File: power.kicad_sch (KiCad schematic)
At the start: 21 parts, among them U10 RT9080-33GJ5, U11 AP22804AW5, U8 TPS2120YFPR, U9 RT9080-33GJ5

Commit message: Membuat library dan memperbaiki footprint pada schematic
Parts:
- U8: footprint Package_BGA:Texas_YFP0020_DSBGA-20_1.56x1.96mm_Layout4x5_P0.4mm -> Package_BGA:Texas_YFP0020_DSBGA-20_1.588x1.988mm_Layout4x5_P0.4mm
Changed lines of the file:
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@@
 			)
 		)
-		(property "Footprint" "Package_BGA:Texas_YFP0020_DSBGA-20_1.56x1.96mm_Layout4x5_P0.4mm"
+		(property "Footprint" "Package_BGA:Texas_YFP0020_DSBGA-20_1.588x1.988mm_Layout4x5_P0.4mm"
 			(at 68.58 83.82 0)
 			(hide yes)

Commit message: Mulai layout
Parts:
- added C46, C49, C50: 100n, Capacitor_SMD:C_0402_1005Metric, symbol Device:C
- added C47, C48: 4u7, Capacitor_SMD:C_0603_1608Metric, symbol Device:C
- added C51: 10u, Capacitor_SMD:C_0603_1608Metric, symbol Device:C
- added D6, D7: SMAJ6.0A, Diode_SMD:D_SMA, symbol Diode:SMAJ6.0A
- added R75, R76: 100k, Resistor_SMD:R_0402_1005Metric, symbol Device:R
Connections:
- net +5V_IN: now also C50.1, C51.1
- net +VBRICK1: now also C46.1, C47.1, D6.1 (A1)
- net +VBRICK2: now also C48.1, C49.1, D7.1 (A1)
- net GND: now also C46.2, C47.2, C48.2, C49.2, C50.2, C51.2, D6.2 (A2), D7.2 (A2), R75.2, R76.2
- net PERI_EN: now also R76.1
- net PWR_SEL: now also R75.1
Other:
- moved on the sheet: C34, C35, C36, C37, C38, C39, C40, C41, D4, R11, R12, R13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

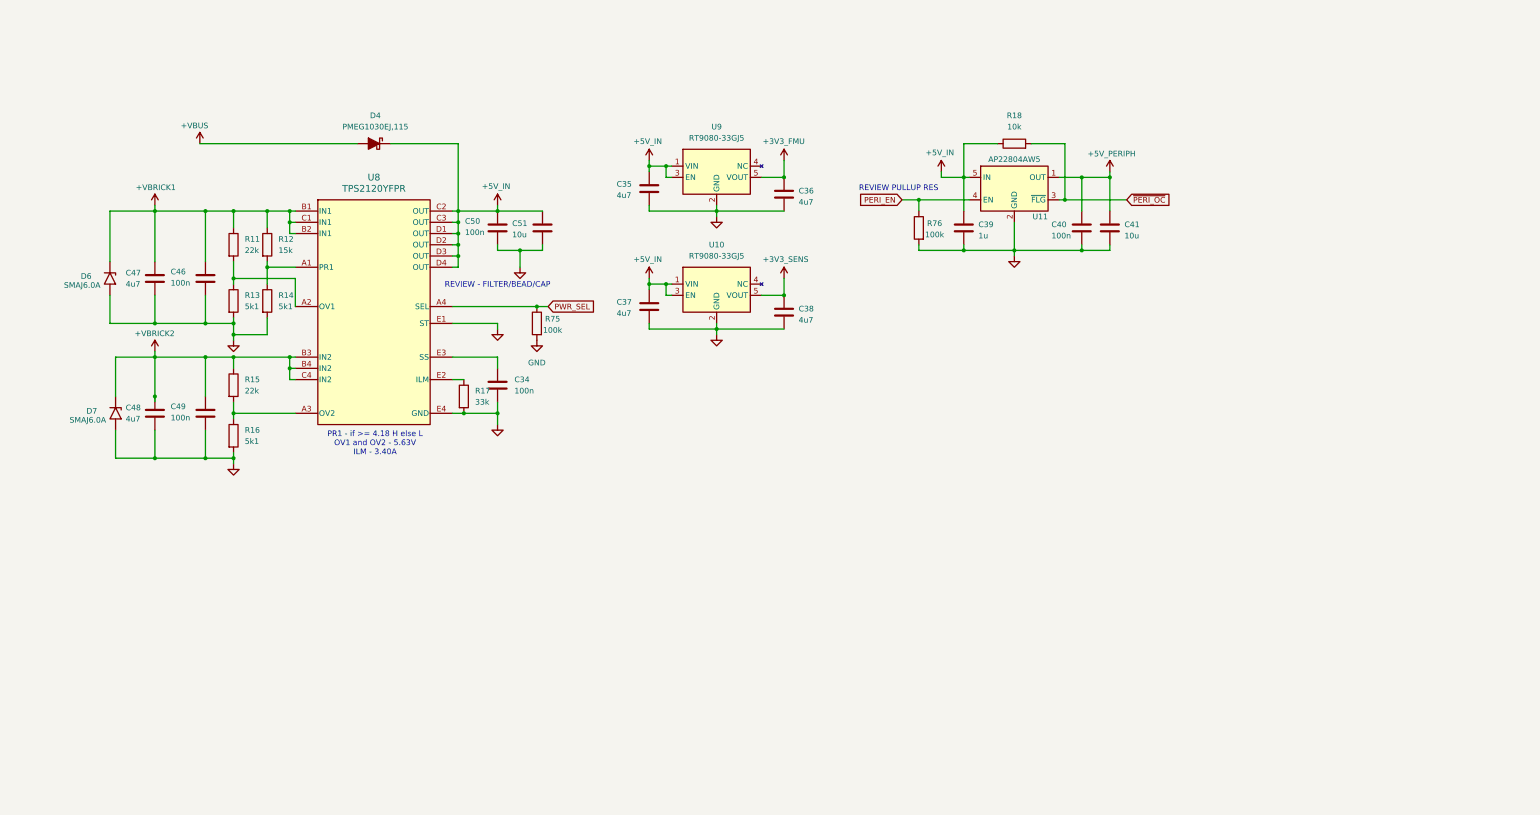
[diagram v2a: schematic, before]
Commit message: Schematic: sensor redundancy + blok current limiter GPS (terverifikasi)
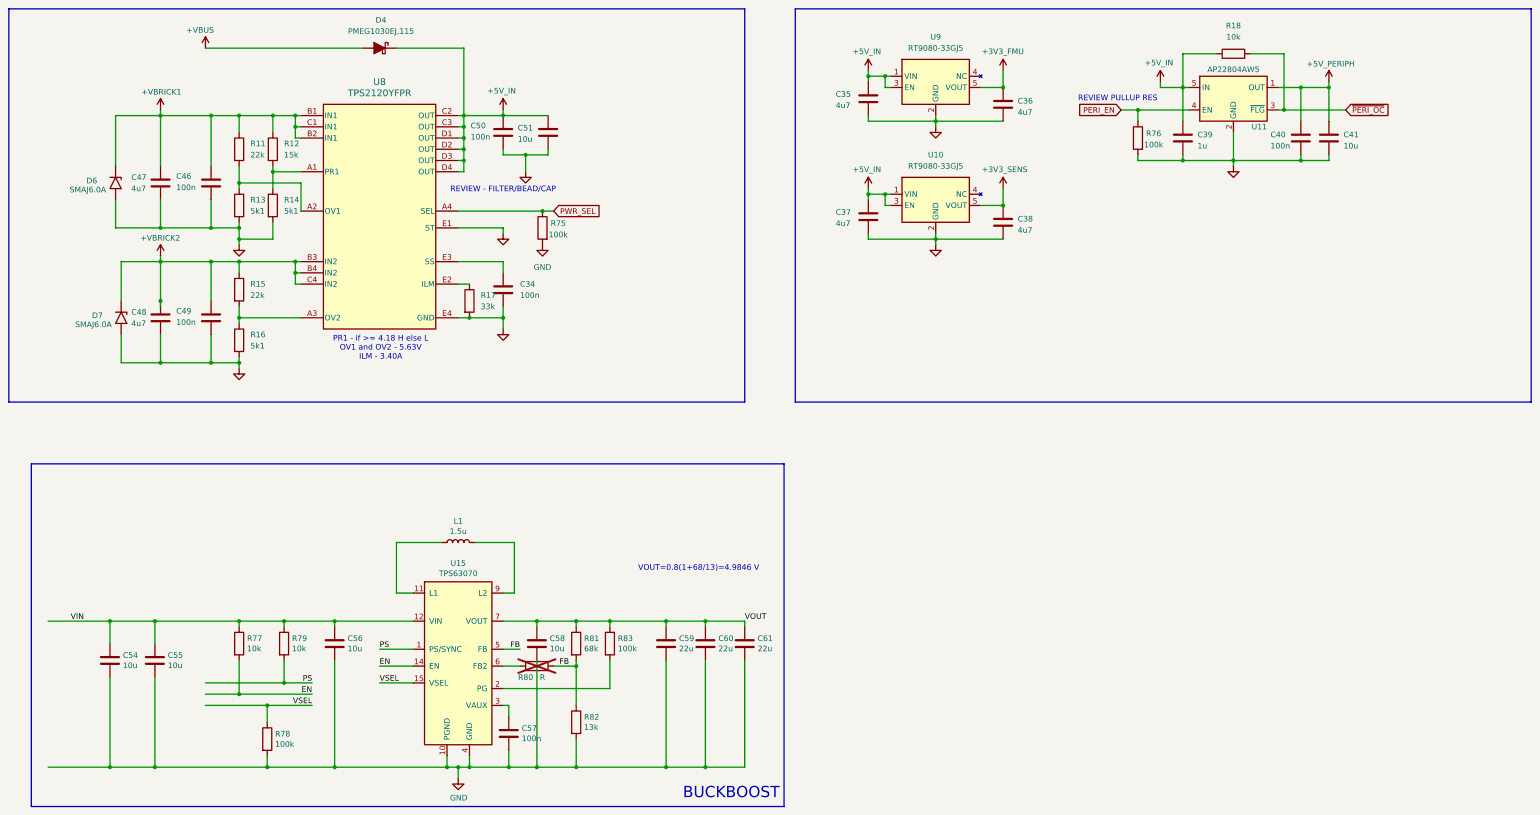
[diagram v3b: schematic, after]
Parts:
- added C54, C55: 10u, Capacitor_SMD:C_0805_2012Metric_Pad1.15x1.40mm_HandSolder, symbol Device:C
- added C56, C58: 10u, Capacitor_SMD:C_0603_1608Metric_Pad1.05x0.95mm_HandSolder, symbol Device:C
- added C57: 100n, Capacitor_SMD:C_0805_2012Metric_Pad1.15x1.40mm_HandSolder, symbol Device:C
- added C59, C60, C61: 22u, Capacitor_SMD:C_0805_2012Metric_Pad1.15x1.40mm_HandSolder, symbol Device:C
- added L1: 1.5u, tps63070:L_Coilcraft_XxL4020, symbol Device:L
- added R77, R79: 10k, Resistor_SMD:R_0805_2012Metric_Pad1.15x1.40mm_HandSolder, symbol Device:R
- added R78, R83: 100k, Resistor_SMD:R_0805_2012Metric_Pad1.15x1.40mm_HandSolder, symbol Device:R
- added R80: R, Resistor_SMD:R_0805_2012Metric_Pad1.15x1.40mm_HandSolder, symbol Device:R
- added R81: 68k, Resistor_SMD:R_0805_2012Metric_Pad1.15x1.40mm_HandSolder, symbol Device:R
- added R82: 13k, Resistor_SMD:R_0805_2012Metric_Pad1.15x1.40mm_HandSolder, symbol Device:R
- added U15: TPS63070, tps63070:VQFN-HR-15, symbol tps63070:tps63070
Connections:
- net GND: now also C54.2, C55.2, C56.2, C57.1, C58.2, C59.2, C60.2, C61.2, R78.2, R82.2, U15.10 (PGND), U15.4 (GND)
- new net: L1.1, U15.11 (L1)
- new net: R83.2, U15.2 (PG)
- new net: C57.2, U15.3 (VAUX)
- new net: R80.2, U15.6 (FB2)
- new net: L1.2, U15.9 (L2)
- new net EN: R77.2, U15.14 (EN)
- new net FB: R80.1, R81.2, R82.1, U15.5 (FB)
- new net PS: R79.2, U15.1 (PS/SYNC)
- new net VIN: C54.1, C55.1, C56.1, R77.1, R79.1, U15.12 (VIN)
- new net VOUT: C58.1, C59.1, C60.1, C61.1, R81.1, R83.1, U15.7 (VOUT)
- new net VSEL: R78.1, U15.15 (VSEL)
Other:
- note added: "BUCKBOOST"
- note added: "VOUT​=0.8(1+68/13)=4.9846 V​"
- moved on the sheet: C34, C35, C36, C37, C38, C39, C40, C41, C46, C47, C48, C49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

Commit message: Power: fix label VIN_BB/EN - U15.VIN kini driven; ERC 54
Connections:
- net VOUT is gone; now on net +5V_IN: C58.1, C59.1, C60.1, C61.1, R81.1, R83.1, U15.7 (VOUT)
- net +5V_IN: no longer C50.1, C51.1, D4.1 (K), U8.C2 (OUT), U8.C3 (OUT), U8.D1 (OUT), U8.D2 (OUT), U8.D3 (OUT), U8.D4 (OUT)
- net VIN renamed VIN_BB
- net VIN_BB: now also C50.1, C51.1, D4.1 (K), U8.C2 (OUT), U8.C3 (OUT), U8.D1 (OUT), U8.D2 (OUT), U8.D3 (OUT), U8.D4 (OUT)
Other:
- note added: "MAX IOUT = 2A"
- moved on the sheet: C54, C55, C56, C57, C58, C59, C60, C61, L1, R77, R78, R79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

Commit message: ERC: R80 DNP+100k+fp, Pin Conflicts Map lengkap; 0 errors / 17 lib-warnings (netlist diff 0, verified)
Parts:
- C54, C55, C57, C59, C60, C61: footprint Capacitor_SMD:C_0805_2012Metric_Pad1.15x1.40mm_HandSolder -> Capacitor_SMD:C_0805_2012Metric
- C56, C58: footprint Capacitor_SMD:C_0603_1608Metric_Pad1.05x0.95mm_HandSolder -> Capacitor_SMD:C_0603_1608Metric
- L1: footprint tps63070:L_Coilcraft_XxL4020 -> Svayam:L_Coilcraft_XxL4020
- R77, R78, R79, R81, R82, R83: footprint Resistor_SMD:R_0805_2012Metric_Pad1.15x1.40mm_HandSolder -> Resistor_SMD:R_0805_2012Metric
- R80: value R -> 100k; footprint Resistor_SMD:R_0805_2012Metric_Pad1.15x1.40mm_HandSolder -> Resistor_SMD:R_0805_2012Metric
- U15: footprint tps63070:VQFN-HR-15 -> Svayam:VQFN-HR-15

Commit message: Annotate: renumber total semua ref (Entire+Reset+X) — netlist 1009 node identik, ERC 0E/17W
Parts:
- renumbered C54 to C40, C55 to C41, C47 to C42, C48 to C43, C46 to C44, C49 to C45, C56 to C46, C57 to C47, C50 to C48, C34 to C49, C58 to C50, C59 to C52, C60 to C53, C61 to C54, C35 to C55, C37 to C56, C36 to C57, C38 to C58, C39 to C59, C40 to C60, C41 to C61, D6 to D4, D7 to D5, D4 to D6, R77 to R15, R11 to R16, R13 to R17, R15 to R18, R16 to R19, R78 to R20, R79 to R21, R12 to R22, R14 to R23, R17 to R24, R80 to R25, R75 to R26, R81 to R27, R82 to R28, R83 to R29, R76 to R30, R18 to R31, U8 to U10, U15 to U11, U9 to U12, U10 to U13, U11 to U14
